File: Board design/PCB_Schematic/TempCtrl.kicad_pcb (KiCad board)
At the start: 4 copper layers, 80 x 100 mm, 184 parts, among them CON1 BARREL_JACK, IC1 ATMEGA328P-A, J1 5V_Outputs_1, J2 External ref, J3 5V_Outputs_2, P1 233-2977, P2 820-8104, P3 RS485, P4 USB_OTG, P5 ICSP, P6 ADC breakout, SW1 DISABLE_COMMS, U1 LM7805, U10 INA330, U11 ISO7242, U12 FT232RL, U13 ADS1262, U14 AD8639, U15 DAC8564, U16 AD8639, U17 DAC8564, U18 74LS125, U2 TMA0505S, U3 ADuM7642CRQZ, U4 ISO3088, U5 OPA548, U6 OPA548, U7 OPA548, U8 OPA548, U9 INA330, X1 TSX-3225 X1E0000210013

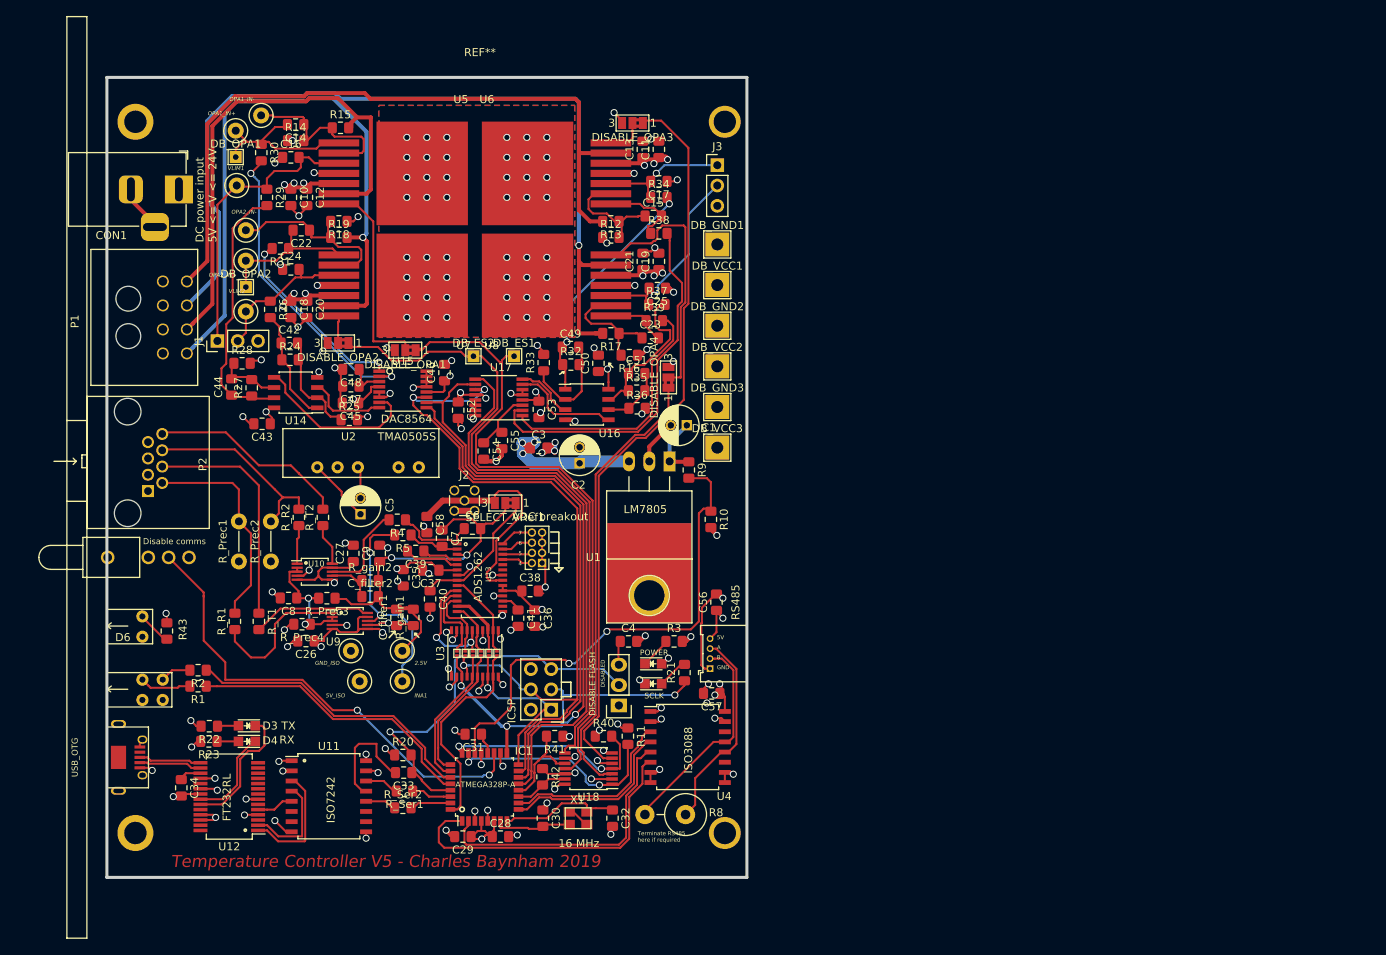
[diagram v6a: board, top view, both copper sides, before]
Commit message: PCB: Mount points
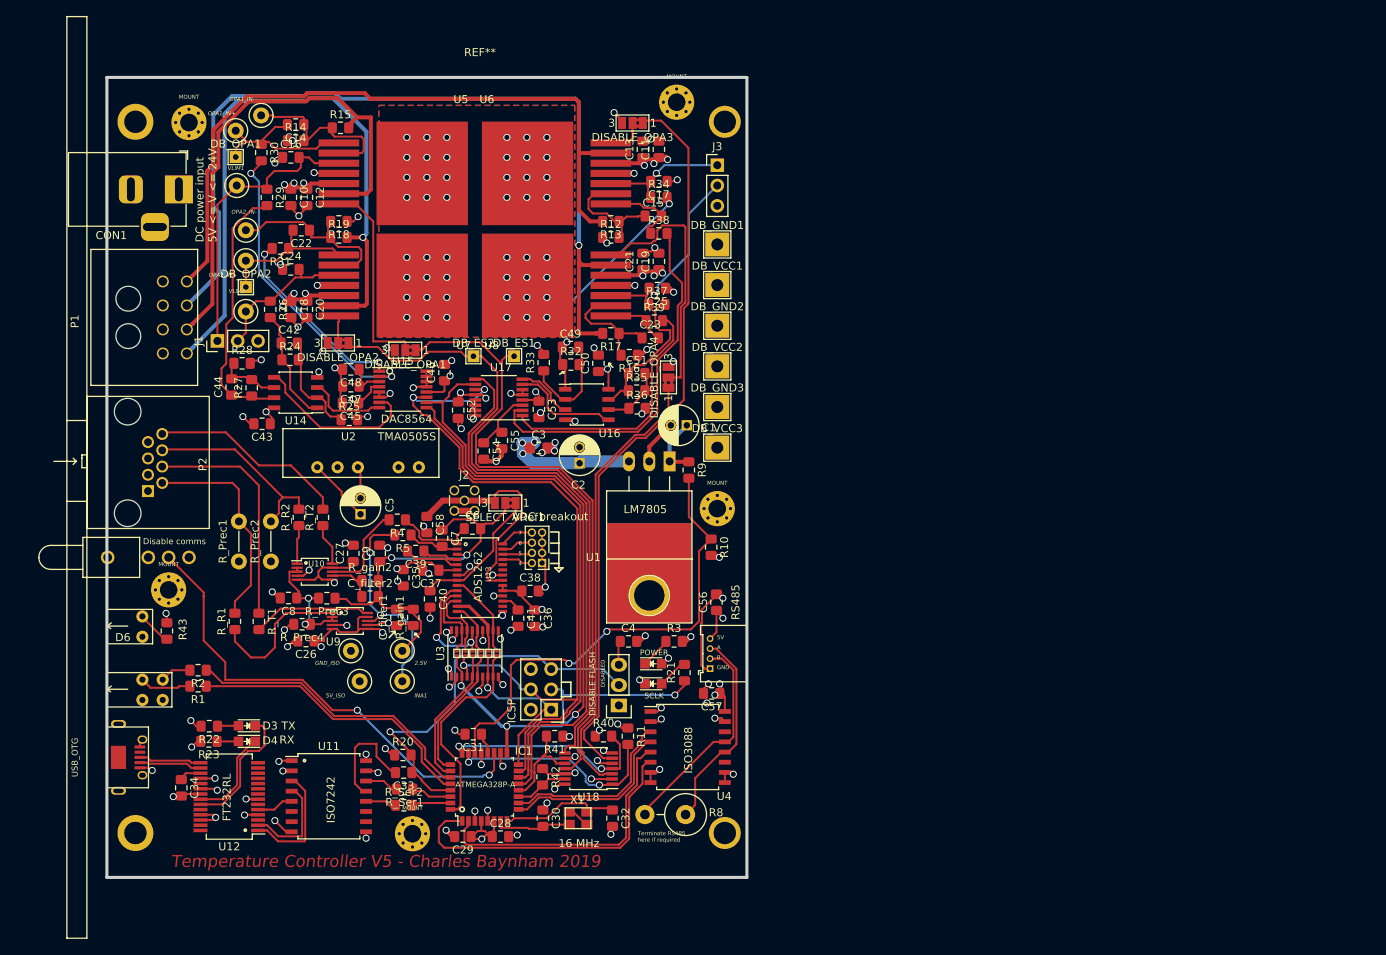
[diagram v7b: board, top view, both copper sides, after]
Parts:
- added MOUNT: MountingHole_2.2mm_M2_Pad_Via, MountingHole:MountingHole_2.2mm_M2_Pad_Via, F.Cu at (175.3, 40.6)
- added MOUNT: MountingHole_2.2mm_M2_Pad_Via, MountingHole:MountingHole_2.2mm_M2_Pad_Via, F.Cu at (241.3, 88.9)
- added MOUNT: MountingHole_2.2mm_M2_Pad_Via, MountingHole:MountingHole_2.2mm_M2_Pad_Via, F.Cu at (172.7, 99.1)
- added MOUNT: MountingHole_2.2mm_M2_Pad_Via, MountingHole:MountingHole_2.2mm_M2_Pad_Via, F.Cu at (203.2, 129.5)
- added MOUNT: MountingHole_2.2mm_M2_Pad_Via, MountingHole:MountingHole_2.2mm_M2_Pad_Via, F.Cu at (236.2, 38.1)
- moved R10 3.48 mm to (240.5, 93.7)
- moved R_Ser2 0.34 mm to (202.1, 126.0)
- moved R_Ser1 0.25 mm to (202.2, 124.0)
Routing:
- net Earth_Clean: track 124.9 -> 120.7 mm
- net /DIYino/A7_inputonly: track 61.6 -> 59.8 mm
- net /C1+_OUT: track 63.8 -> 63.0 mm
- net /C3+_OUT: track 90.0 -> 89.1 mm
- net /RS485_GND: track 18.2 -> 17.4 mm
- net /C4+_OUT: track 110.1 -> 109.5 mm

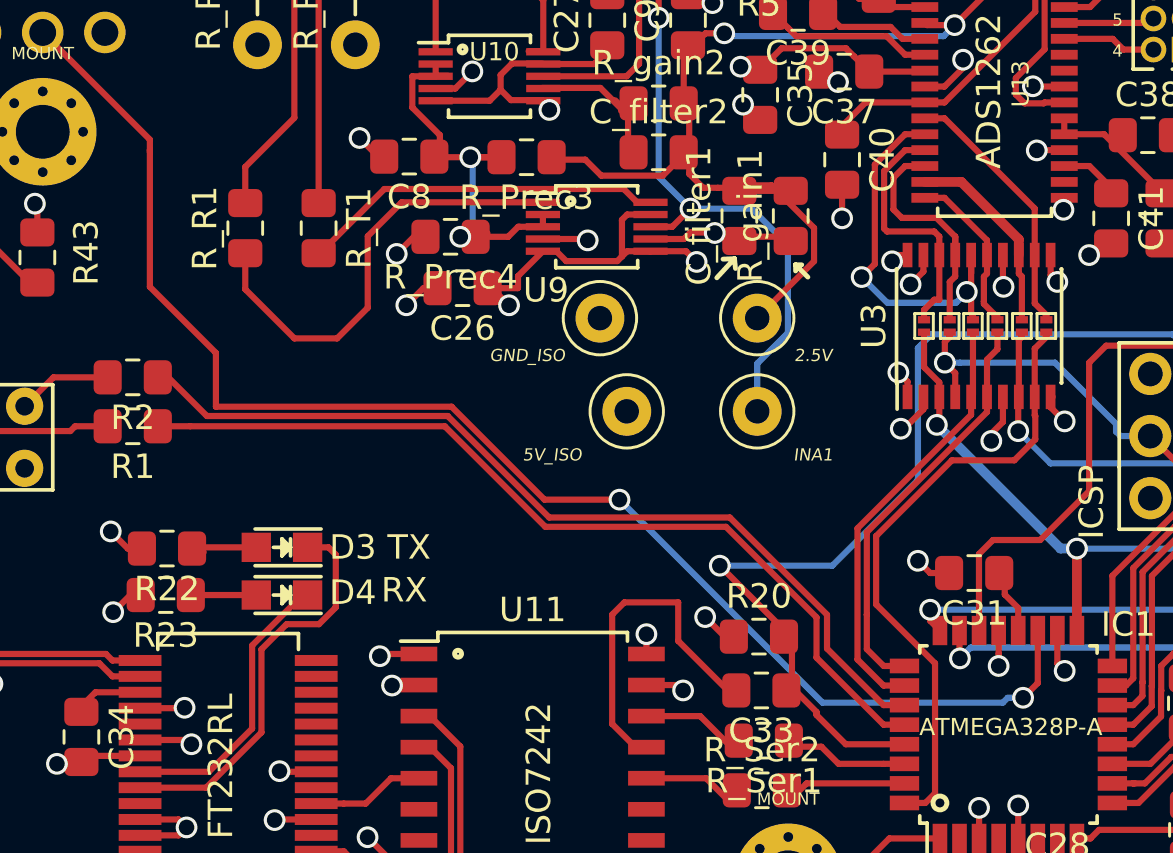
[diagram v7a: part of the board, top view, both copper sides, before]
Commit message: BOTH: Add 5V daughterboard point
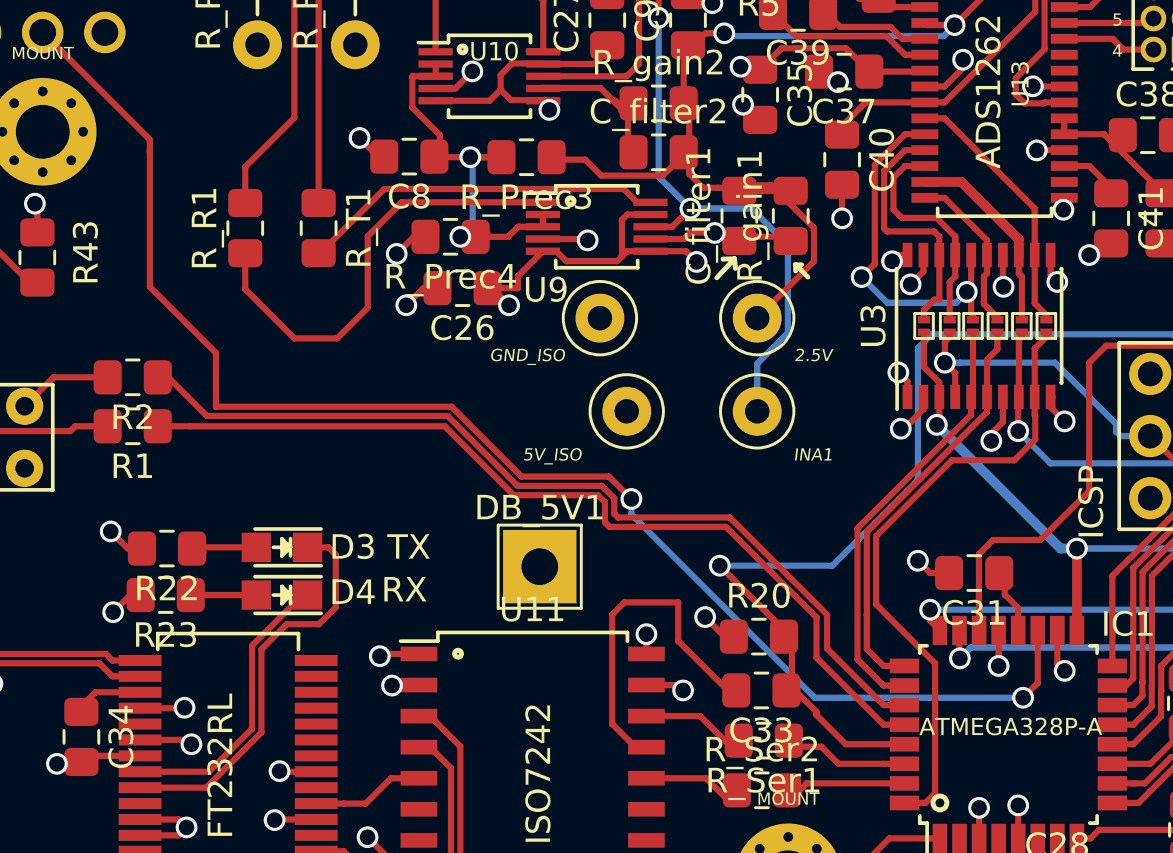
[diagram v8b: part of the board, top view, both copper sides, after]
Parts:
- added DB_5V1: PIN, TestPoint:TestPoint_THTPad_3.0x3.0mm_Drill1.5mm, F.Cu at (193.0, 116.8)
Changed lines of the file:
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@@
     (thickness 1.6)
     (drawings 54)
-    (tracks 1903)
+    (tracks 1912)
     (zones 0)
-    (modules 189)
+    (modules 190)
     (nets 156)
   )
@@
     (diff_pair_gap 0.25)
   )
+  (module TestPoint:TestPoint_THTPad_3.0x3.0mm_Drill1.5mm (layer F.Cu)
+    (at 193.04 116.84)
+    (descr "THT rectangular pad as test Point, square 3.0mm side length, hole diameter 1.5mm")
+    (tags "test point THT pad rectangle square")
+    (attr virtual)
+    (fp_text reference DB_5V1 (at 0 -2.398) (layer F.SilkS)
+      (effects (font (size 1 1) (thickness 0.15)))
+    )
+    (fp_text value PIN (at 0 2.55) (layer F.Fab)
+      (effects (font (size 1 1) (thickness 0.15)))
+    )
+    (fp_line (start 2 2) (end -2 2) (layer F.CrtYd) (width 0.05))
+    (fp_line (start 2 2) (end 2 -2) (layer F.CrtYd) (width 0.05))
+    (fp_line (start -2 -2) (end -2 2) (layer F.CrtYd) (width 0.05))
+    (fp_line (start -2 -2) (end 2 -2) (layer F.CrtYd) (width 0.05))
+    (fp_line (start -1.7 1.7) (end -1.7 -1.7) (layer F.SilkS) (width 0.12))
+    (fp_line (start 1.7 1.7) (end -1.7 1.7) (layer F.SilkS) (width 0.12))
+    (fp_line (start 1.7 -1.7) (end 1.7 1.7) (layer F.SilkS) (width 0.12))
+    (fp_line (start -1.7 -1.7) (end 1.7 -1.7) (layer F.SilkS) (width 0.12))
+    (fp_text user %R (at 0 -2.4) (layer F.Fab)
+      (effects (font (size 1 1) (thickness 0.15)))
+    )
+    (pad 1 thru_hole rect (at 0 0) (size 3 3) (drill 1.5) (layers *.Cu *.Mask)
+      (net 4 +5V))
+  )
   (module MountingHole:MountingHole_2.2mm_M2_Pad_Via (layer F.Cu)
     (at 175.26 40.64)
@@
   (segment (start 207.096 121.7) (end 206.029968 120.633968) (width 0.254) (layer F.Cu) (net 78))
   (segment (start 210.75 107.45) (end 210.75 107.254) (width 0.254) (layer F.Cu) (net 78))
-  (segment (start 177.75 109.1) (end 177.85 109.1) (width 0.254) (layer F.Cu) (net 79) (status 30))
-  (segment (start 177.85 109.1) (end 179.431011 110.681011) (width 0.254) (layer F.Cu) (net 79) (status 10))
+  (segment (start 195.57814 113.53798) (end 196.08802 114.04786) (width 0.254) (layer F.Cu) (net 79))
+  (segment (start 196.238848 114.829968) (end 200.811532 114.829968) (width 0.254) (layer F.Cu) (net 79))
+  (segment (start 207.096 122.5) (end 207.95 122.5) (width 0.254) (layer F.Cu) (net 79))
+  (segment (start 204.783969 118.802405) (end 204.783969 120.187969) (width 0.254) (layer F.Cu) (net 79))
+  (segment (start 177.75 109.1) (end 177.85 109.1) (width 0.254) (layer F.Cu) (net 79))
   (segment (start 204.783969 120.187969) (end 207.096 122.5) (width 0.254) (layer F.Cu) (net 79))
-  (segment (start 207.096 122.5) (end 207.95 122.5) (width 0.254) (layer F.Cu) (net 79) (status 20))
+  (segment (start 196.08802 114.67914) (end 196.238848 114.829968) (width 0.254) (layer F.Cu) (net 79))
   (segment (start 200.811532 114.829968) (end 204.783969 118.802405) (width 0.254) (layer F.Cu) (net 79))
-  (segment (start 204.783969 118.802405) (end 204.783969 120.187969) (width 0.254) (layer F.Cu) (net 79))
-  (segment (start 193.426064 114.829968) (end 200.811532 114.829968) (width 0.254) (layer F.Cu) (net 79))
-  (segment (start 189.277107 110.681011) (end 193.426064 114.829968) (width 0.254) (layer F.Cu) (net 79))
   (segment (start 179.431011 110.681011) (end 189.277107 110.681011) (width 0.254) (layer F.Cu) (net 79))
-  (segment (start 207.95 123.3) (end 207.096 123.3) (width 0.254) (layer F.Cu) (net 80) (status 10))
-  (segment (start 193.268245 115.210979) (end 189.157266 111.1) (width 0.254) (layer F.Cu) (net 80))
-  (segment (start 200.653713 115.210979) (end 193.268245 115.210979) (width 0.254) (layer F.Cu) (net 80))
+  (segment (start 196.08802 114.04786) (end 196.08802 114.67914) (width 0.254) (layer F.Cu) (net 79))
+  (segment (start 192.134076 113.53798) (end 195.57814 113.53798) (width 0.254) (layer F.Cu) (net 79))
+  (segment (start 177.85 109.1) (end 179.431011 110.681011) (width 0.254) (layer F.Cu) (net 79))
+  (segment (start 189.277107 110.681011) (end 192.134076 113.53798) (width 0.254) (layer F.Cu) (net 79))
+  (segment (start 178.754 111.1) (end 177.75 111.1) (width 0.254) (layer F.Cu) (net 80))
+  (segment (start 189.157266 111.1) (end 178.754 111.1) (width 0.254) (layer F.Cu) (net 80))
+  (segment (start 191.976257 113.918991) (end 189.157266 111.1) (width 0.254) (layer F.Cu) (net 80))
+  (segment (start 195.420321 113.918991) (end 191.976257 113.918991) (width 0.254) (layer F.Cu) (net 80))
+  (segment (start 195.707009 114.205679) (end 195.420321 113.918991) (width 0.254) (layer F.Cu) (net 80))
+  (segment (start 195.707009 115.031179) (end 195.707009 114.205679) (width 0.254) (layer F.Cu) (net 80))
   (segment (start 204.354001 120.558001) (end 204.354001 118.911267) (width 0.254) (layer F.Cu) (net 80))
+  (segment (start 195.886809 115.210979) (end 195.707009 115.031179) (width 0.254) (layer F.Cu) (net 80))
   (segment (start 204.354001 118.911267) (end 200.653713 115.210979) (width 0.254) (layer F.Cu) (net 80))
-  (segment (start 189.157266 111.1) (end 178.754 111.1) (width 0.254) (layer F.Cu) (net 80))
-  (segment (start 178.754 111.1) (end 177.75 111.1) (width 0.254) (layer F.Cu) (net 80) (status 20))
+  (segment (start 207.95 123.3) (end 207.096 123.3) (width 0.254) (layer F.Cu) (net 80))
   (segment (start 207.096 123.3) (end 204.354001 120.558001) (width 0.254) (layer F.Cu) (net 80))
+  (segment (start 200.653713 115.210979) (end 195.886809 115.210979) (width 0.254) (layer F.Cu) (net 80))
   (segment (start 208.804 126.5) (end 207.95 126.5) (width 0.254) (layer F.Cu) (net 81) (status 20))
   (segment (start 209.2 126.104) (end 208.804 126.5) (width 0.254) (layer F.Cu) (net 81))
@@
   (segment (start 177.1 99.38) (end 172.72 95) (width 0.254) (layer F.Cu) (net 90) (status 20))
   (segment (start 177.1 99.9) (end 177.1 99.8) (width 0.254) (layer F.Cu) (net 90))
-  (segment (start 177.1 105.4) (end 177.1 99.8) (width 0.254) (layer F.Cu) (net 90))
-  (segment (start 193.234926 114.1) (end 189.434926 110.3) (width 0.254) (layer F.Cu) (net 90))
-  (segment (start 189.434926 110.3) (end 179.8 110.3) (width 0.254) (layer F.Cu) (net 90))
-  (segment (start 196.3 114.1) (end 193.234926 114.1) (width 0.254) (layer F.Cu) (net 90))
-  (segment (start 179.8 110.3) (end 179.8 108.1) (width 0.254) (layer F.Cu) (net 90))
-  (segment (start 179.8 108.1) (end 177.1 105.4) (width 0.254) (layer F.Cu) (net 90))
-  (segment (start 196.3 114.1) (end 196.5 114.3) (width 0.254) (layer F.Cu) (net 90))
-  (segment (start 211.971383 122.4) (end 204.6 122.4) (width 0.254) (layer B.Cu) (net 90))
-  (segment (start 204.6 122.4) (end 196.3 114.1) (width 0.254) (layer B.Cu) (net 90))
-  (via (at 196.3 114.1) (size 0.889) (drill 0.635) (layers F.Cu B.Cu) (net 90))
-  (segment (start 212.8 122.2) (end 212.171383 122.2) (width 0.254) (layer B.Cu) (net 90))
-  (segment (start 212.171383 122.2) (end 211.971383 122.4) (width 0.254) (layer B.Cu) (net 90))
   (via (at 212.8 122.2) (size 0.889) (drill 0.635) (layers F.Cu B.Cu) (net 90))
   (segment (start 213.4 121.6) (end 212.8 122.2) (width 0.254) (layer F.Cu) (net 90))
   (segment (start 213.4 119.45) (end 213.4 121.6) (width 0.254) (layer F.Cu) (net 90) (status 10))
+  (via (at 196.78653 114.072494) (size 0.889) (drill 0.635) (layers F.Cu B.Cu) (net 90))
+  (segment (start 212.8 122.2) (end 204.285419 122.2) (width 0.254) (layer B.Cu) (net 90))
+  (segment (start 204.285419 122.2) (end 196.78653 114.701111) (width 0.254) (layer B.Cu) (net 90))
+  (segment (start 196.78653 114.701111) (end 196.78653 114.072494) (width 0.254) (layer B.Cu) (net 90))
+  (segment (start 192.291895 113.156969) (end 195.871005 113.156969) (width 0.254) (layer F.Cu) (net 90))
+  (segment (start 196.727506 114.072494) (end 196.78653 114.072494) (width 0.254) (layer F.Cu) (net 90))
+  (segment (start 195.871005 113.156969) (end 196.78653 114.072494) (width 0.254) (layer F.Cu) (net 90))
+  (segment (start 189.434926 110.3) (end 192.291895 113.156969) (width 0.254) (layer F.Cu) (net 90))
+  (segment (start 177.1 99.8) (end 177.1 105.4) (width 0.254) (layer F.Cu) (net 90))
+  (segment (start 179.8 110.3) (end 189.434926 110.3) (width 0.254) (layer F.Cu) (net 90))
+  (segment (start 179.8 108.1) (end 179.8 110.3) (width 0.254) (layer F.Cu) (net 90))
+  (segment (start 177.1 105.4) (end 179.8 108.1) (width 0.254) (layer F.Cu) (net 90))
+  (segment (start 196.5 114.3) (end 196.727506 114.072494) (width 0.254) (layer F.Cu) (net 90))
   (segment (start 212.05 117.1) (end 212.05 117.979) (width 0.254) (layer F.Cu) (net 91) (status 10))
   (segment (start 212.05 117.979) (end 212.6 118.529) (width 0.254) (layer F.Cu) (net 91))
